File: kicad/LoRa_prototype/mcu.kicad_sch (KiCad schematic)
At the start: 18 parts, among them U1 STM32WL55JCIx, X1 32768Hz

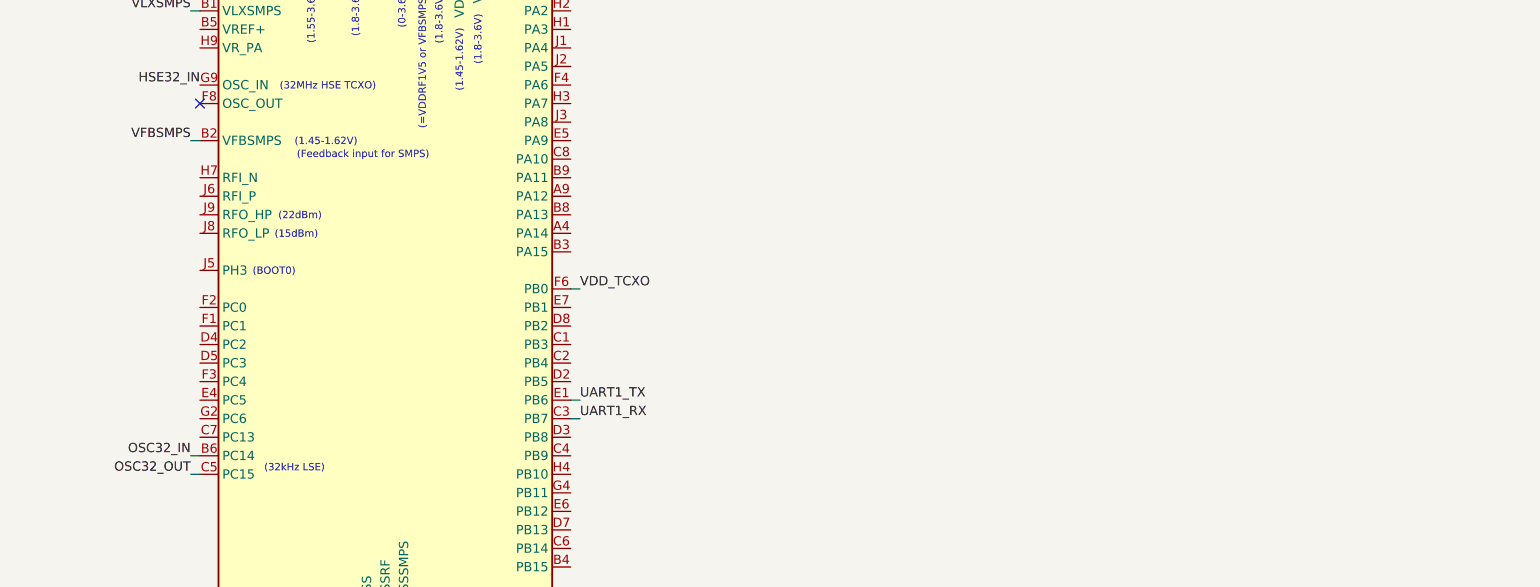
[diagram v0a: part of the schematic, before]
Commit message: Done RF matching network in schematic
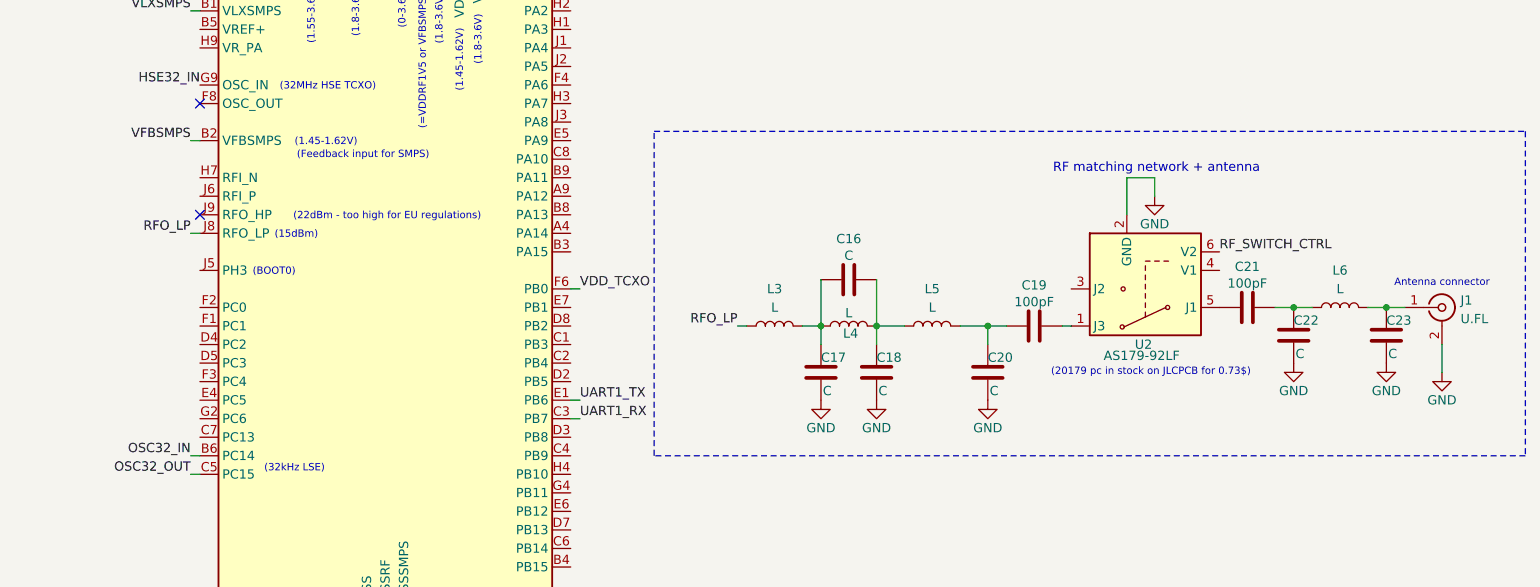
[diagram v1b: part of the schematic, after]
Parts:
- added C16, C17, C18, C20, C22, C23: C, symbol Device:C
- added C19, C21: 100pF, symbol Device:C
- added J1: U.FL, PCM_JLCPCB:IPEX-SMD_BWIPX-1-001E, symbol PCM_JLCPCB-Extended:RF, Connector, U.FL
- added L3, L4, L5, L6: L, symbol Device:L
- added U2: AS179-92LF, Package_TO_SOT_SMD:SOT-363_SC-70-6, symbol RF_Switch:AS179-92LF
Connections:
- net GND: now also C17.2, C18.2, C20.2, C22.2, C23.2, J1.2 (Ext), U2.2 (GND)
- net RFO_LP: now reaches U1.J8 (RFO_LP)
- net RFO_LP: now also L3.1
- new net: C21.1, U2.5 (J1)
- new net: C21.2, C22.1, L6.1
- new net: C16.1, C17.1, L3.2, L4.1
- new net: C16.2, C18.1, L4.2, L5.1
- new net: C19.1, C20.1, L5.2
- new net: C19.2, U2.1 (J3)
- new net: C23.1, J1.1 (In), L6.2
- new net RF_SWITCH_CTRL: U2.6 (V2)
- no-connect marks 1 -> 2
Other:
- note added: "(20179 pc in stock on JLCPCB for 0.73$)"
- note added: "(22dBm - too high for EU regulations)"
- note added: "Antenna connector"
- note added: "RF matching network + antenna"
- note removed: "(22dBm)"
- company: (none) -> DesCap GmbH
- title: (none) -> STM32WL55

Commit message: Stable commit
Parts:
- removed C22, C23: C, symbol Device:C
- removed L6: L, symbol Device:L
- added C15: 47nF, symbol Device:C
- added C24, C29: 68pF, symbol Device:C
- added C25: 3pF, symbol Device:C
- added C26: 2.2pF, symbol Device:C
- added C28: 100pF, symbol Device:C
- added L2: 47nH, symbol Device:L
- added L7: 12nH, symbol Device:L
- C16: value C -> 3.3pF
- C17: value C -> 7.7pF
- C18: value C -> 3.6pF
- C20: value C -> 1.4pF
- L3: value L -> 3.5nH
- L4: value L -> 2.6nH
- L5: value L -> 7.5nH
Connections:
- net GND: now also C15.2, C24.2, C25.2
- net at C21.2: now also J1.1 (In)
- net at C16.1, C17.1, L3.2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: now also L2.2
- net at C16.2, C18.1, L4.2: now also C29.1; no longer L5.1
- net TX: now reaches C19.1, C20.1, L5.2
- net at U2.3 (J2): now also C28.2
- net RF_SWITCH_CTRL_V1: now reaches U2.4 (V1)
- net RFI_N: now reaches U1.H7 (RFI_N)
- net RFI_N: now also C25.1, L7.2
- net VR_PA: now reaches U1.H9 (VR_PA)
- net VR_PA: now also C15.1, C24.1, L2.1
- net RFI_P: now reaches U1.J6 (RFI_P)
- net RFI_P: now also C26.1, L7.1
- net RF_SWITCH_CTRL renamed RF_SWITCH_CTRL_V2
- new net: C29.2, L5.1
- new net RX: C26.2, C28.1
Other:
- note added: "(IL=0.3dB)"
- note added: "(V_HIGH: 2-5V)"
- note added: "RF switch + antenna"
- note removed: "(20179 pc in stock on JLCPCB for 0.73$)"
- note removed: "RF matching network + antenna"
- moved on the sheet: C10, C16, C17, C18, C20, J1, L3, L4, L5, U1

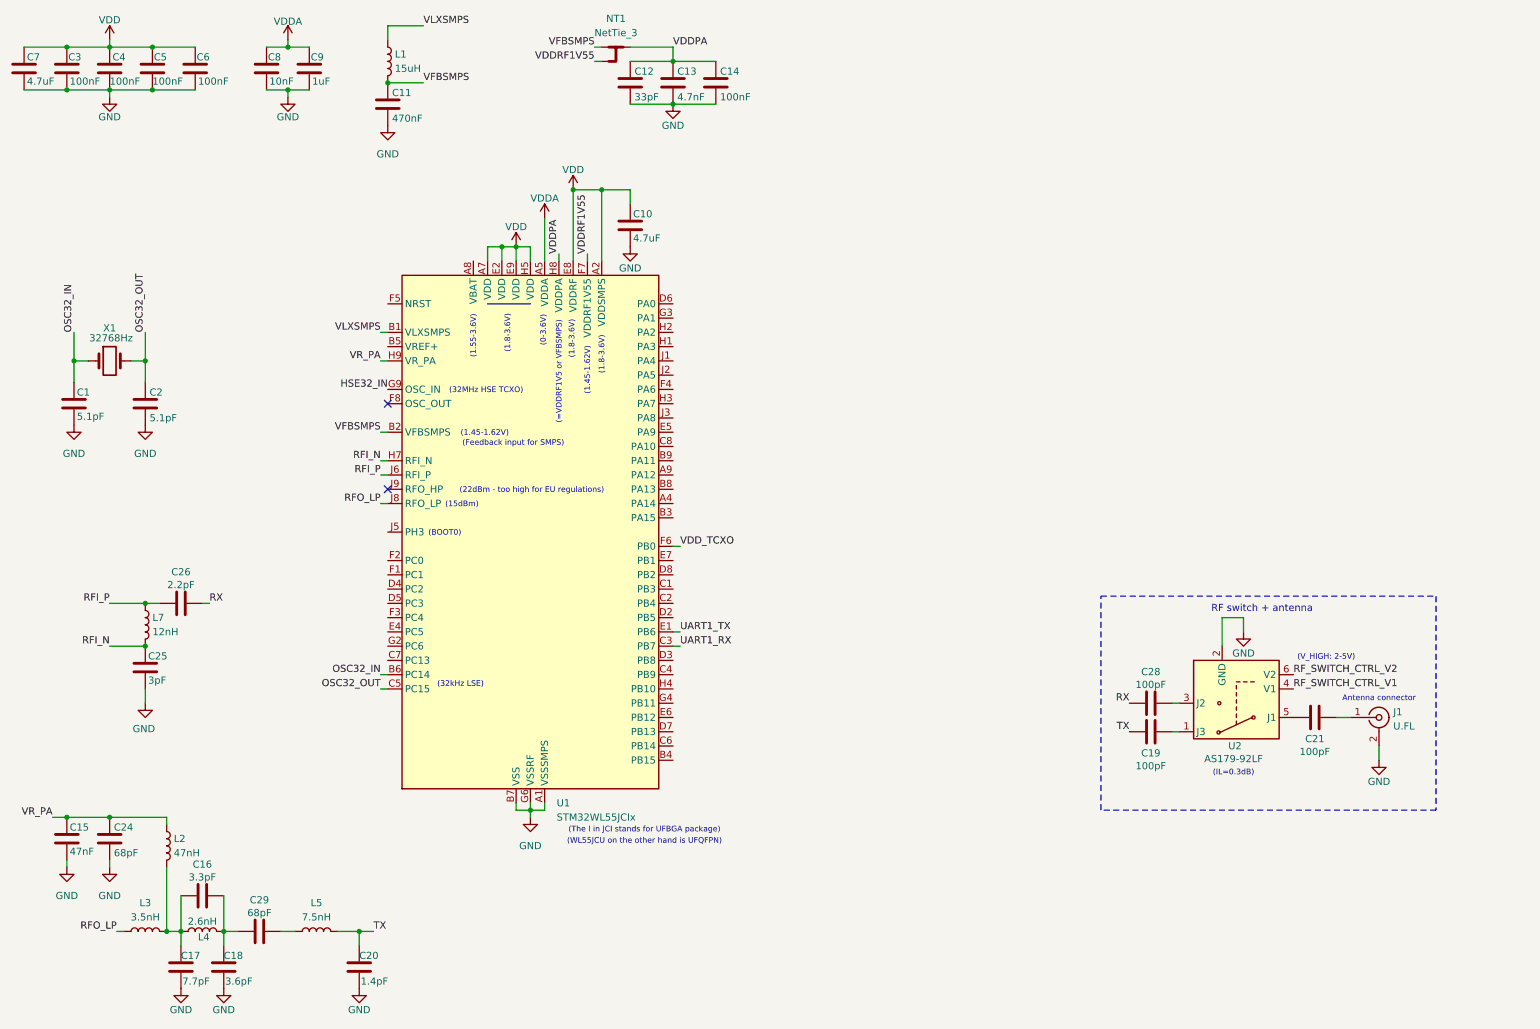
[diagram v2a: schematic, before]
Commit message: Reorganized schematic
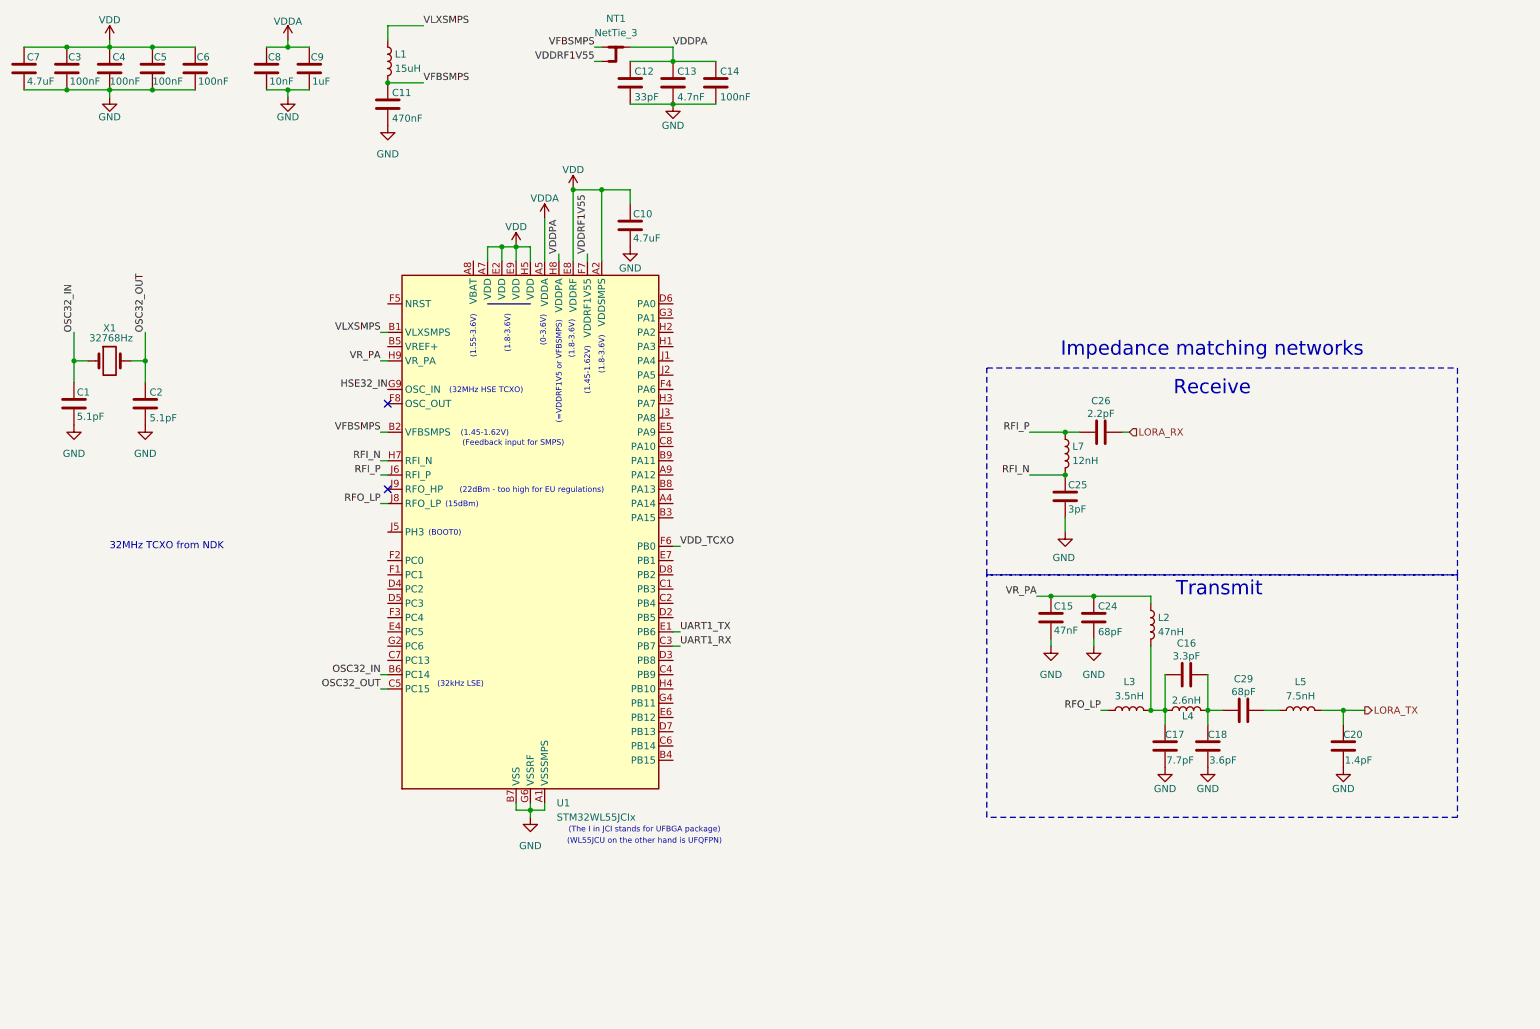
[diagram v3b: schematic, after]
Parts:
- removed C19, C21, C28: 100pF, symbol Device:C
- removed J1: U.FL, PCM_JLCPCB:IPEX-SMD_BWIPX-1-001E, symbol PCM_JLCPCB-Extended:RF, Connector, U.FL
- removed U2: AS179-92LF, Package_TO_SOT_SMD:SOT-363_SC-70-6, symbol RF_Switch:AS179-92LF
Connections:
- net RX renamed LORA_RX
- net TX renamed LORA_TX
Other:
- note added: "32MHz TCXO from NDK"
- note added: "Impedance matching networks"
- note added: "Receive"
- note added: "Transmit"
- note removed: "(IL=0.3dB)"
- note removed: "(V_HIGH: 2-5V)"
- note removed: "Antenna connector"
- note removed: "RF switch + antenna"
- moved on the sheet: C15, C16, C17, C18, C20, C24, C25, C26, C29, L2, L3, L4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

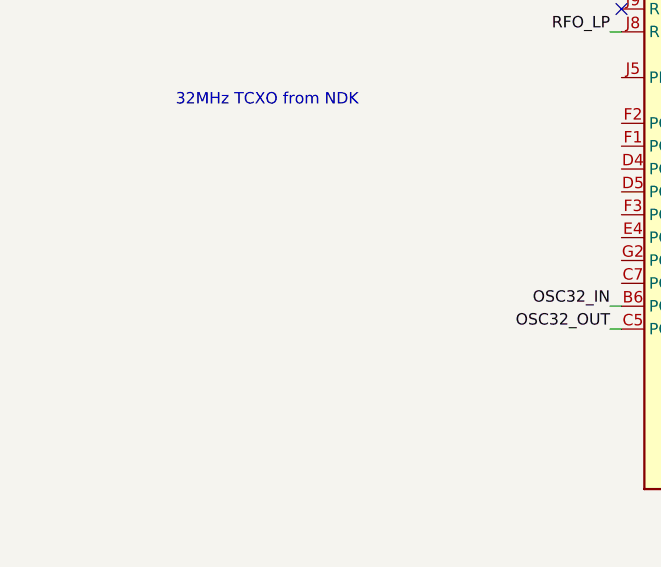
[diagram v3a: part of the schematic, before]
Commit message: Added custom TCXO symbol
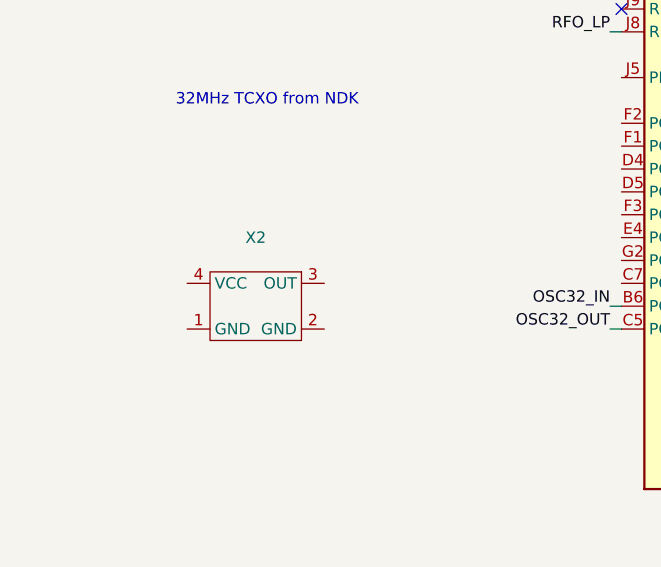
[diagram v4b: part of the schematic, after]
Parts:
- added X2: ~, symbol Custom:TCXO_NT2016SF
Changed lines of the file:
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@@
+	)
+	(symbol
+		(lib_id "Custom:TCXO_NT2016SF")
+		(at 39.37 133.35 0)
+		(unit 1)
+		(exclude_from_sim no)
+		(in_bom yes)
+		(on_board yes)
+		(dnp no)
+		(fields_autoplaced yes)
+		(property "Reference" "X2"
+			(at 39.37 125.73 0)
+			(effects
+				(font
+					(size 1.27 1.27)
+				)
+			)
+		)
+		(property "Value" "~"
+			(at 39.37 128.27 0)
+			(effects
+				(font
+					(size 1.27 1.27)
+				)
+			)
+		)
+		(property "Footprint" ""
+			(at 39.37 133.35 0)
+			(effects
+				(font
+					(size 1.27 1.27)
+				)
+				(hide yes)
+			)
+		)
+		(property "Datasheet" ""
+			(at 39.37 133.35 0)
+			(effects
+				(font
+					(size 1.27 1.27)
+				)
+				(hide yes)
+			)
+		)
+		(property "Description" ""
+			(at 39.37 133.35 0)
+			(effects
+				(font
+					(size 1.27 1.27)
+				)
+				(hide yes)
+			)
+		)
+		(pin "1"
+		)
+		(pin "3"
+		)
+		(pin "2"
+		)
+		(pin "4"
+		)
+		(instances
+			(project ""
+				(path "/9fad4700-f514-47ad-821a-b4076ecc08de/aff57de4-7349-43c5-ba7a-251ada06728f"
+					(reference "X2")
+					(unit 1)
+				)
+			)
+		)
 	)
 	(symbol

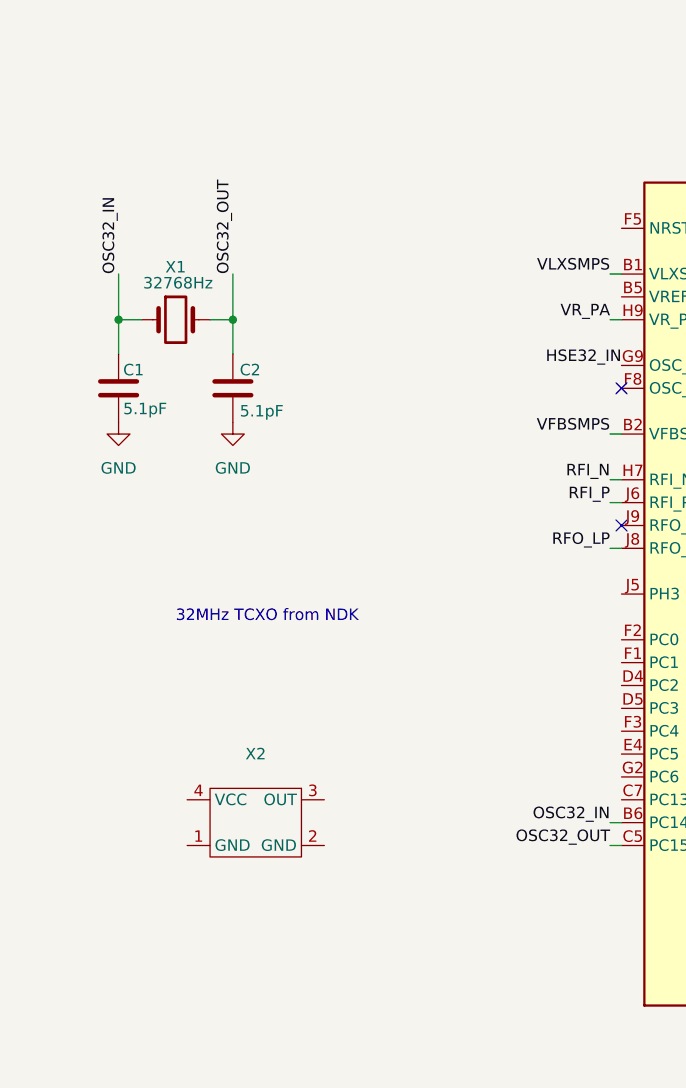
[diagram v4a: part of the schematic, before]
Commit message: Added LSE and HSE crystals to schematic
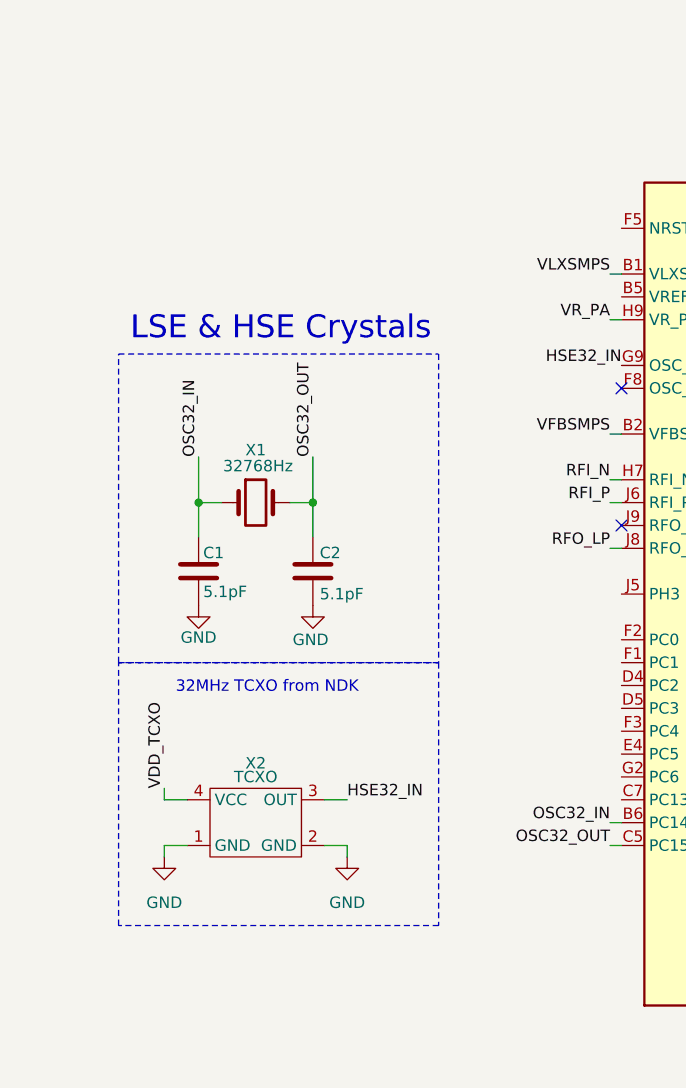
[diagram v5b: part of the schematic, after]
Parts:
- X2: value ~ -> TCXO
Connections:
- net GND: now also X2.1 (GND), X2.2 (GND)
- net HSE32_IN: now also X2.3 (OUT)
- net VDD_TCXO: now also X2.4 (VCC)
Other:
- note added: "LSE & HSE Crystals"
- moved on the sheet: C1, C2, X1

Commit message: Done doing MCU schematic (Milestone)
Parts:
- added C19, C21: 1nF, symbol Device:C
- added C28: 100nF, symbol Device:C
- added R1: 10K, symbol Device:R
- added SW1: SW_Push, symbol Switch:SW_Push
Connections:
- net GND: now also U1.J5 (PH3), C19.2, C28.2, SW1.2
- net HSE32_IN: now also C21.2; no longer X2.3 (OUT)
- net VDD: now also U1.A8 (VBAT), R1.1
- net VDDA: now also U1.B5 (VREF+)
- net VDD_TCXO: now also C19.1
- net NRST: now reaches U1.F5 (NRST)
- net NRST: now also C28.1, R1.2, SW1.1
- new net: C21.1, X2.3 (OUT)
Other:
- note added: "(Always boot from main flash)"
- note added: "Reset"
- moved on the sheet: C1, C2, L1, X1, X2
